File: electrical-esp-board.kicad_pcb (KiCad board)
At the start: 2 copper layers, 155.1 x 125.1 mm, 60 parts, among them J1 pH, J10 General IO, J11 MC1, J12 12v switch, J13 MC2, J14 Limit Switch, J15 5v switch, J16 Limit Switch, J2 Generic Analog, J3 FLow Sensor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

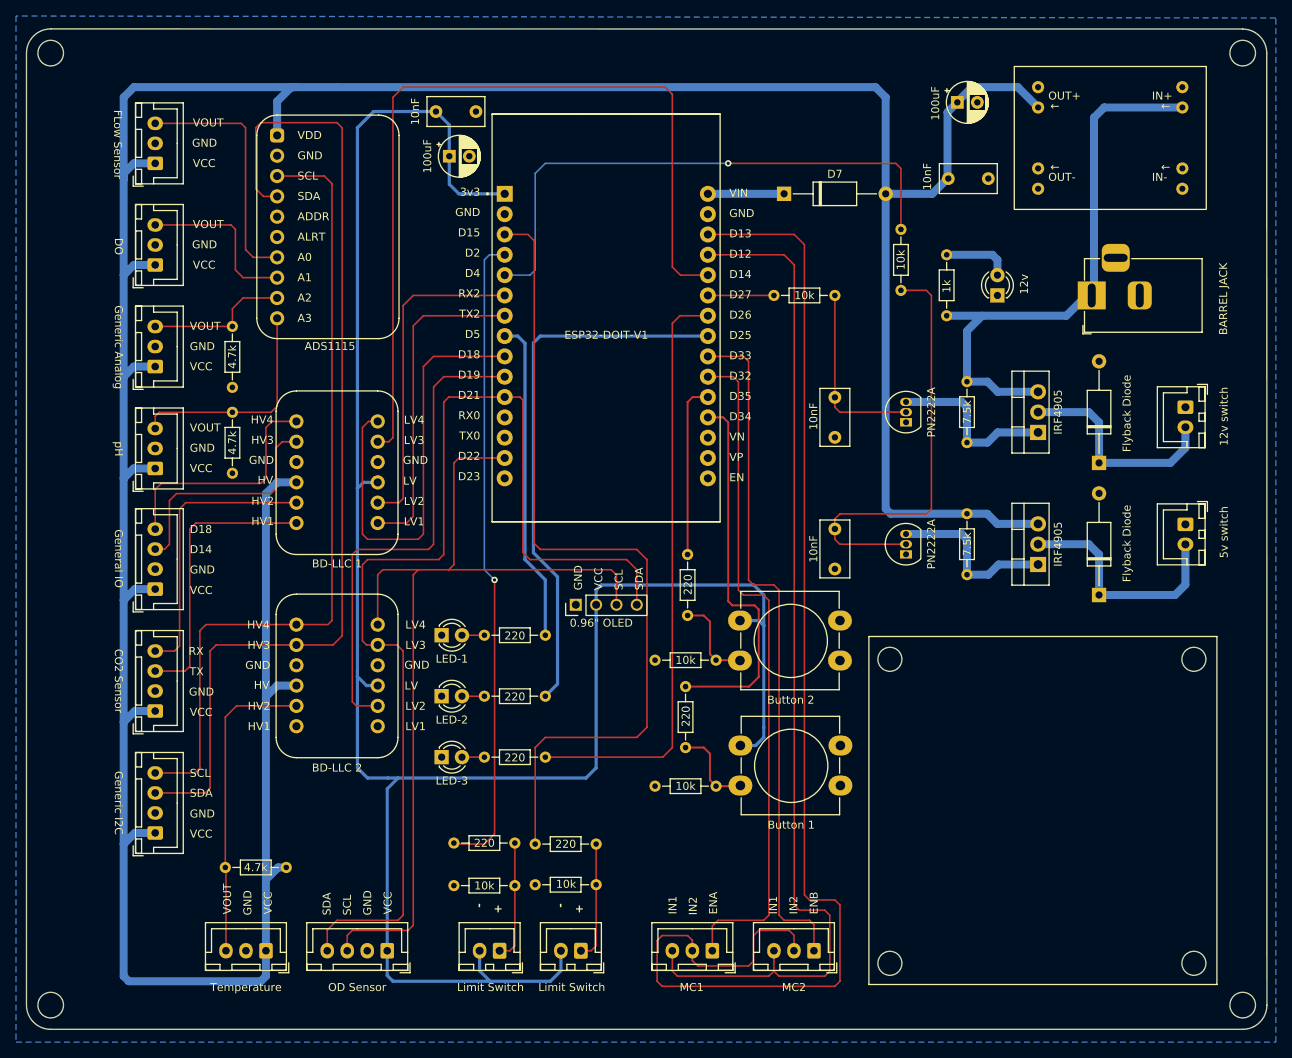
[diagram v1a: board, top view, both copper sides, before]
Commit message: removed uneeded JSP pins ready for it to be worked on
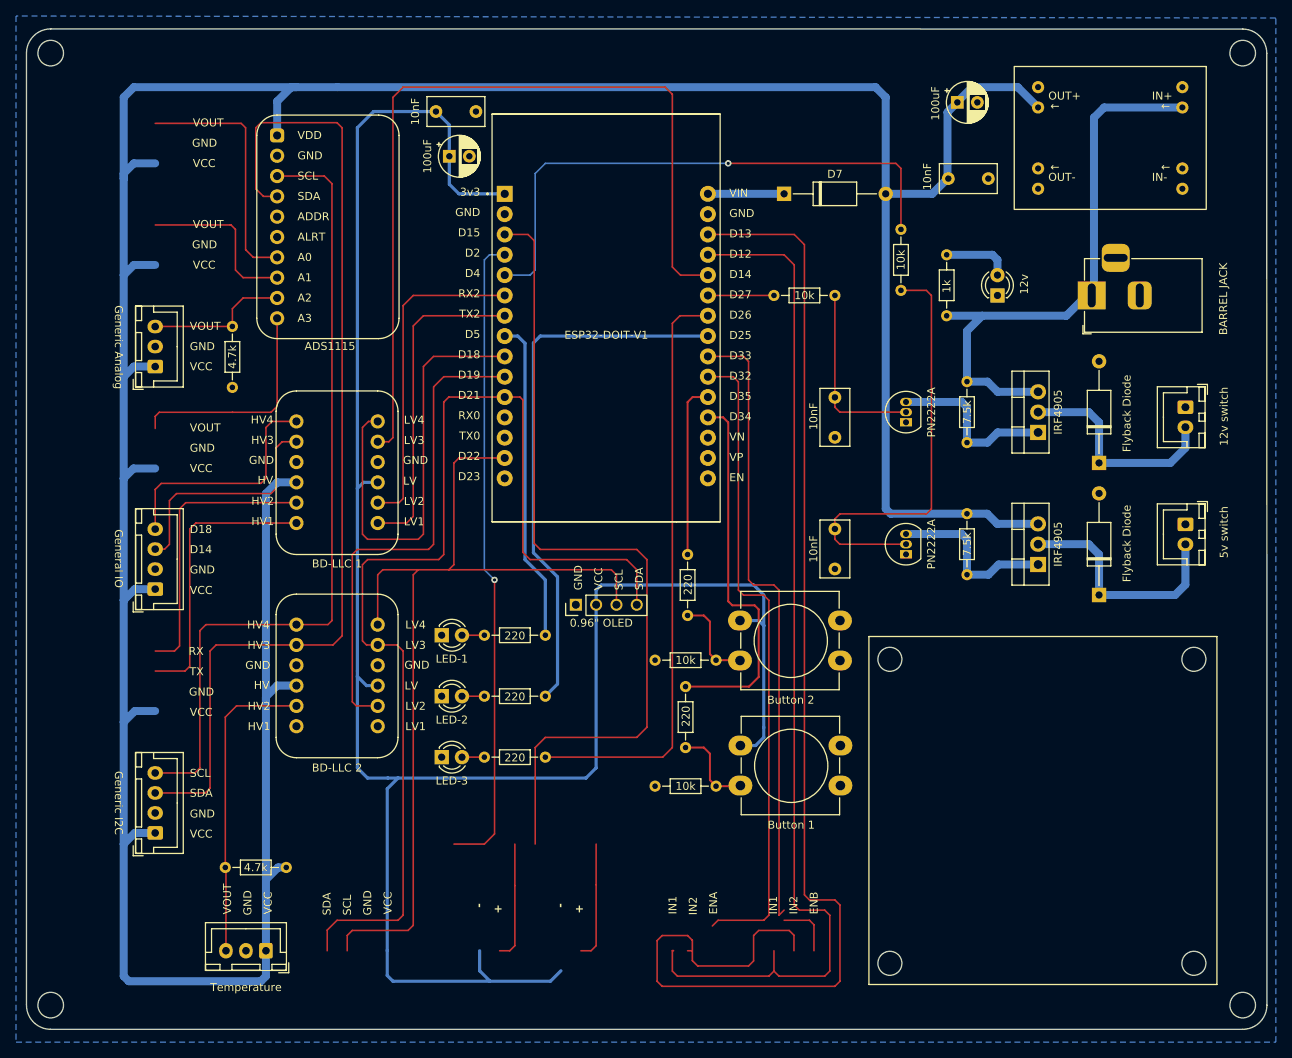
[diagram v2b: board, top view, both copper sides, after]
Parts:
- removed J1: pH, Connector_JST:JST_XH_B3B-XH-A_1x03_P2.50mm_Vertical
- removed J11: MC1, Connector_JST:JST_XH_B3B-XH-A_1x03_P2.50mm_Vertical
- removed J13: MC2, Connector_JST:JST_XH_B3B-XH-A_1x03_P2.50mm_Vertical
- removed J14, J16: Limit Switch, Connector_JST:JST_XH_B2B-XH-A_1x02_P2.50mm_Vertical
- removed J3: FLow Sensor, Connector_JST:JST_XH_B3B-XH-A_1x03_P2.50mm_Vertical
- removed J4: DO, Connector_JST:JST_XH_B3B-XH-A_1x03_P2.50mm_Vertical
- removed J5: OD Sensor, Connector_JST:JST_XH_B4B-XH-A_1x04_P2.50mm_Vertical
- removed J9: CO2 Sensor, Connector_JST:JST_XH_B4B-XH-A_1x04_P2.50mm_Vertical
- removed R1: 4.7k, Resistor_THT:R_Axial_DIN0204_L3.6mm_D1.6mm_P7.62mm_Horizontal
- removed R11, R14: 220, Resistor_THT:R_Axial_DIN0204_L3.6mm_D1.6mm_P7.62mm_Horizontal
- removed R12, R15: 10k, Resistor_THT:R_Axial_DIN0204_L3.6mm_D1.6mm_P7.62mm_Horizontal
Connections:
- U1 pad 4: VOUT-FL -> unconnected-(U1-A0-Pad4)
- U1 pad 5: VOUT-DO -> unconnected-(U1-A1-Pad5)
- U1 pad 7: VOUT-PH -> unconnected-(U1-A3-Pad7)
- U3 pad 21: D32 -> unconnected-(U3-D32-Pad21)
- U3 pad 22: D33 -> unconnected-(U3-D33-Pad22)
- U3 pad 27: D12 -> unconnected-(U3-D12-Pad27)
- U3 pad 28: D13 -> unconnected-(U3-D13-Pad28)
- U3 pad 3: D15 -> unconnected-(U3-D15-Pad3)
- U3 pad 4: D2 -> unconnected-(U3-D2-Pad4)
- U3 pad 6: RX-LV -> unconnected-(U3-RX2-Pad6)
- U3 pad 7: TX-LV -> unconnected-(U3-TX2-Pad7)
- U4 pad 1: TX-HV -> unconnected-(U4-HV1-Pad1)
- U4 pad 2: RX-HV -> unconnected-(U4-HV2-Pad2)
- U4 pad 7: TX-LV -> unconnected-(U4-LV1-Pad7)
- U4 pad 8: RX-LV -> unconnected-(U4-LV2-Pad8)
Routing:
- net unconnected-(U3-D13-Pad28): track 0.00 -> 163.8 mm
- net D13: track 163.8 -> 0.00 mm
- net unconnected-(U3-D12-Pad27): track 0.00 -> 129.2 mm
- net D12: track 129.2 -> 0.00 mm
- net (no net): track 0.00 -> 111.0 mm
- net unconnected-(U3-D15-Pad3): track 0.00 -> 104.8 mm
- net D15: track 104.8 -> 0.00 mm
- net D33: track 85.7 -> 0.00 mm
- net unconnected-(U3-D33-Pad22): track 0.00 -> 85.7 mm
- net D32: track 84.5 -> 0.00 mm
- net unconnected-(U3-D32-Pad21): track 0.00 -> 81.4 mm
- net unconnected-(U3-D2-Pad4): track 0.00 -> 80.7 mm, vias 0 -> 1
- net D2: track 80.7 -> 0.00 mm, vias 1 -> 0
- net RX-LV: track 40.7 -> 0.00 mm
- net TX-LV: track 40.6 -> 0.00 mm
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
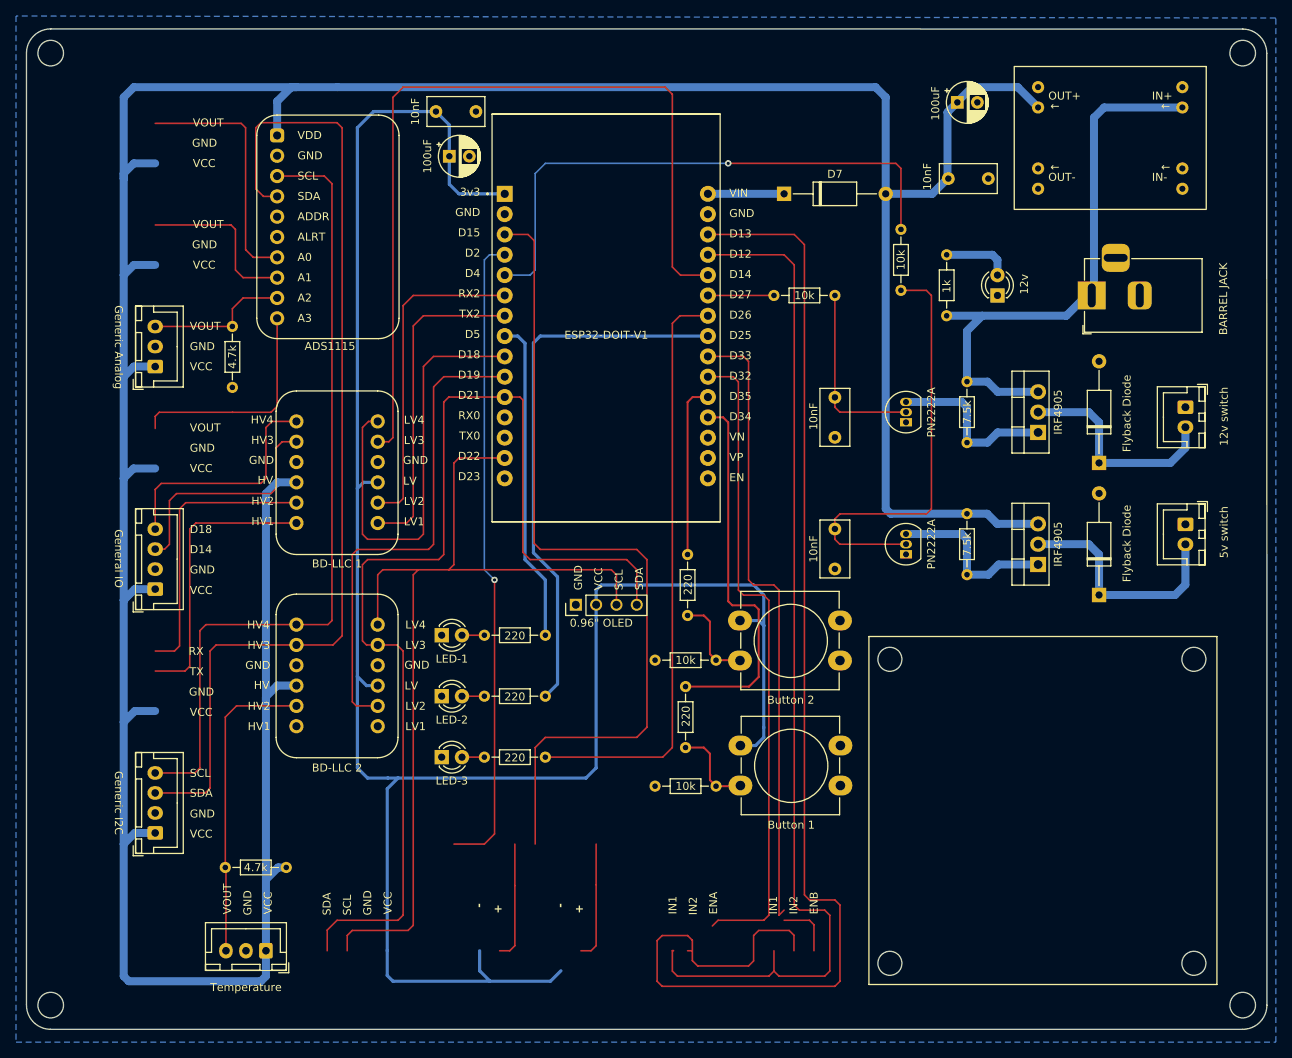
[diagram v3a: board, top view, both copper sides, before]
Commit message: Cleaned up and added rest of JSTs
removed all of the extra wires and unneeded components. added the footprints of all of the temp sensors and 3 extra I2Cs. aren't in correct position or wired up as of yet
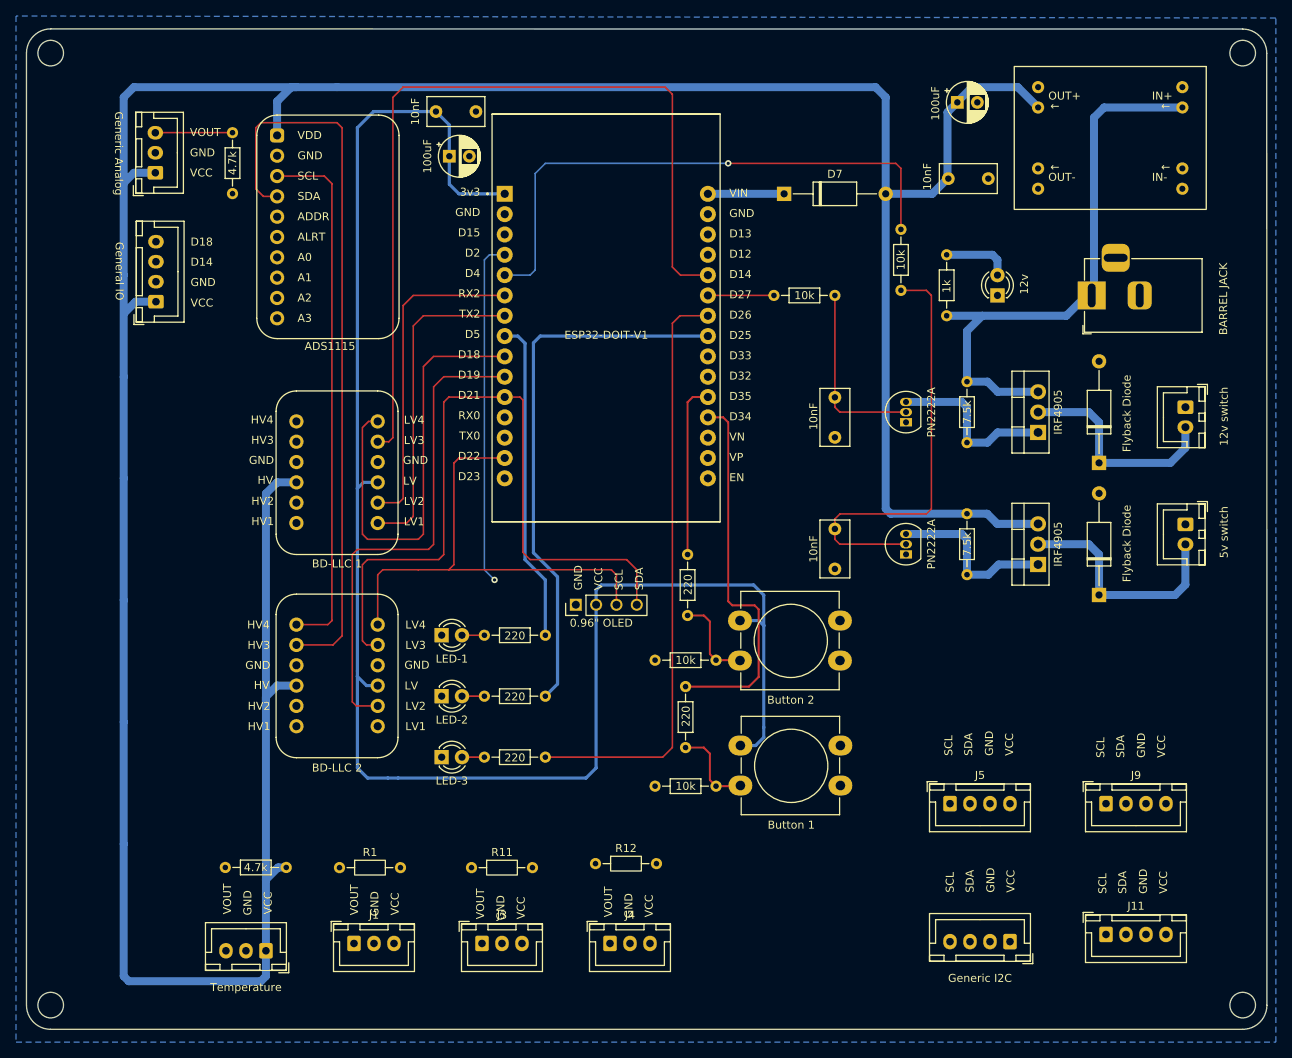
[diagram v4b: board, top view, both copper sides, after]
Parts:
- added J1: Temperature, Connector_JST:JST_XH_B3B-XH-A_1x03_P2.50mm_Vertical, F.Cu at (98.0, 135.0)
- added J11: IMU, Connector_JST:JST_XH_B4B-XH-A_1x04_P2.50mm_Vertical, F.Cu at (192.0, 133.8)
- added J3: Temperature, Connector_JST:JST_XH_B3B-XH-A_1x03_P2.50mm_Vertical, F.Cu at (114.0, 135.0)
- added J4: Temperature, Connector_JST:JST_XH_B3B-XH-A_1x03_P2.50mm_Vertical, F.Cu at (130.0, 135.0)
- added J5: Pressure, Connector_JST:JST_XH_B4B-XH-A_1x04_P2.50mm_Vertical, F.Cu at (172.5, 117.5)
- added J9: IMU, Connector_JST:JST_XH_B4B-XH-A_1x04_P2.50mm_Vertical, F.Cu at (192.0, 117.5)
- added R1: 4.7k, Resistor_THT:R_Axial_DIN0204_L3.6mm_D1.6mm_P7.62mm_Horizontal, F.Cu at (96.2, 125.5)
- added R11: 4.7k, Resistor_THT:R_Axial_DIN0204_L3.6mm_D1.6mm_P7.62mm_Horizontal, F.Cu at (112.7, 125.5)
- added R12: 4.7k, Resistor_THT:R_Axial_DIN0204_L3.6mm_D1.6mm_P7.62mm_Horizontal, F.Cu at (128.2, 125.0)
- moved J7 107.7 mm to (180.0, 134.8), turned to 180 degrees
- moved J10 35.9 mm to (73.2, 54.8)
- moved J2 24.2 mm to (73.2, 38.6)
- moved R2 24.2 mm to (82.8, 33.6)
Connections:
- net VOUT-TEMP-HV renamed VOUT-TEMP-HV-1
- net VOUT-TEMP-LV renamed VOUT-TEMP-LV-1
- U2 pad 1: unconnected-(U2-HV1-Pad1) -> VOUT-TEMP-HV-2
- U2 pad 7: unconnected-(U2-LV1-Pad7) -> VOUT-TEMP-LV-2
- U3 pad 21: unconnected-(U3-D32-Pad21) -> VOUT-TEMP-LV-2
- U3 pad 22: unconnected-(U3-D33-Pad22) -> VOUT-TEMP-LV-3
- U3 pad 28: unconnected-(U3-D13-Pad28) -> VOUT-TEMP-LV-4
- U4 pad 1: unconnected-(U4-HV1-Pad1) -> VOUT-TEMP-HV-4
- U4 pad 2: unconnected-(U4-HV2-Pad2) -> VOUT-TEMP-HV-3
- U4 pad 7: unconnected-(U4-LV1-Pad7) -> VOUT-TEMP-LV-4
- U4 pad 8: unconnected-(U4-LV2-Pad8) -> VOUT-TEMP-LV-3
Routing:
- net unconnected-(U3-D13-Pad28): track 163.8 -> 0.00 mm
- net unconnected-(U3-D12-Pad27): track 129.2 -> 0.00 mm
- net (no net): track 111.0 -> 0.00 mm
- net unconnected-(U3-D15-Pad3): track 104.8 -> 0.00 mm
- net unconnected-(U3-D33-Pad22): track 85.7 -> 0.00 mm
- net unconnected-(U3-D32-Pad21): track 81.4 -> 0.00 mm
- net SCL: track 115.9 -> 60.5 mm
- net +3V3: track 265.1 -> 213.0 mm
- net SDA: track 139.6 -> 90.2 mm
- net unconnected-(U3-RX2-Pad6): track 0.00 -> 40.7 mm
- net unconnected-(U3-TX2-Pad7): track 0.00 -> 40.6 mm
- net VOUT-TEMP-HV-1: track 38.8 -> 0.19 mm
- net unconnected-(U3-D2-Pad4): track 80.7 -> 43.3 mm
- net unconnected-(U4-HV2-Pad2): track 35.4 -> 0.00 mm
- net SCL-HV: track 101.9 -> 66.5 mm
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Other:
- outline, holes or cut-outs redrawn
- board text removed: "+"
- board text removed: "-"
- board text removed: "ENA"
- board text removed: "ENB"
- board text removed: "IN1"
- board text removed: "IN2"
- board text removed: "RX"
- board text removed: "TX"

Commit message: Moved all JST to proposed locations, unwired
Moved all of the JSTs to the proposed locations. Waiting to be checked so I can wire it afterwards
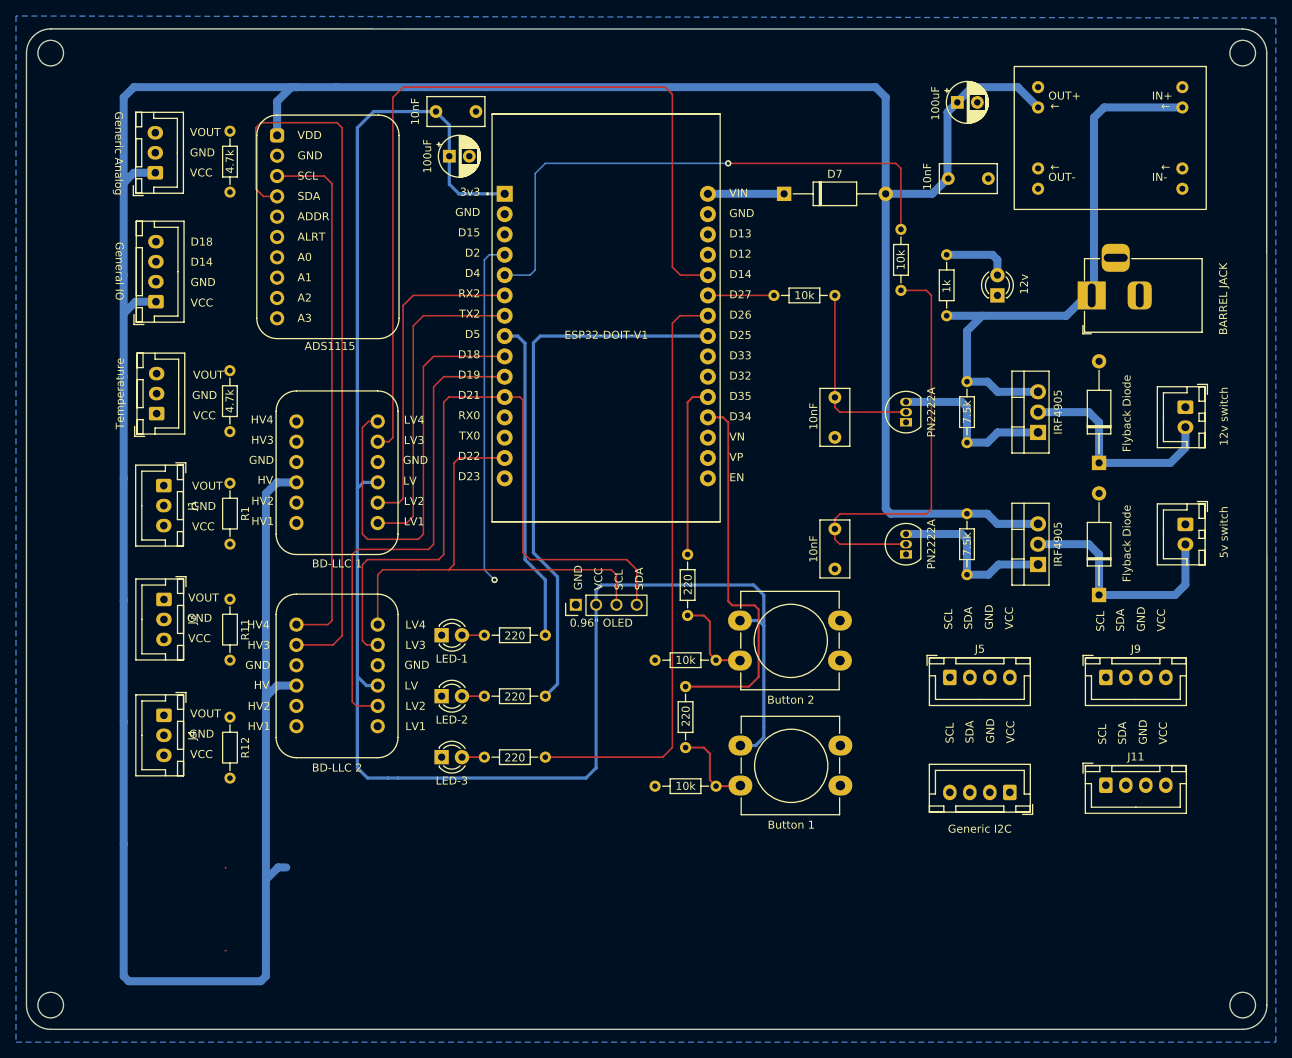
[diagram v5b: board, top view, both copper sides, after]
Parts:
- moved J6 68.5 mm to (73.3, 68.7), turned to 90 degrees
- moved J4 62.6 mm to (74.2, 106.5), turned to -90 degrees
- moved R3 62.1 mm to (82.5, 63.4), turned to -90 degrees
- moved J1 62.0 mm to (74.2, 77.7), turned to -90 degrees
- moved J3 58.6 mm to (74.2, 92.0), turned to -90 degrees
- moved R1 50.0 mm to (82.5, 77.4), turned to -90 degrees
- moved R12 49.2 mm to (82.5, 106.7), turned to -90 degrees
- moved R11 45.1 mm to (82.5, 91.9), turned to -90 degrees
- moved J11 18.7 mm to (192.0, 115.2)
- moved J7 18.7 mm to (180.0, 116.1)
- moved J5 15.8 mm to (172.5, 101.7)
- moved J9 15.8 mm to (192.0, 101.7)
- moved R2 0.37 mm to (82.5, 33.4)
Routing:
- net VOUT-GA: track 9.74 -> 0.11 mm
